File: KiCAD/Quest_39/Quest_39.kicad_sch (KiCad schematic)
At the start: 58 parts, among them J1 1x2 Scr. Term., J10 1x2 Scr. Term., J11 1x2 Scr. Term., J12 Conn_01x05_Male, J2 1x2 Scr. Term., J3 1x2 Scr. Term., J4 1x2 Scr. Term., J5 1x2 Scr. Term., J6 1x2 Scr. Term., J7 1x2 Scr. Term.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

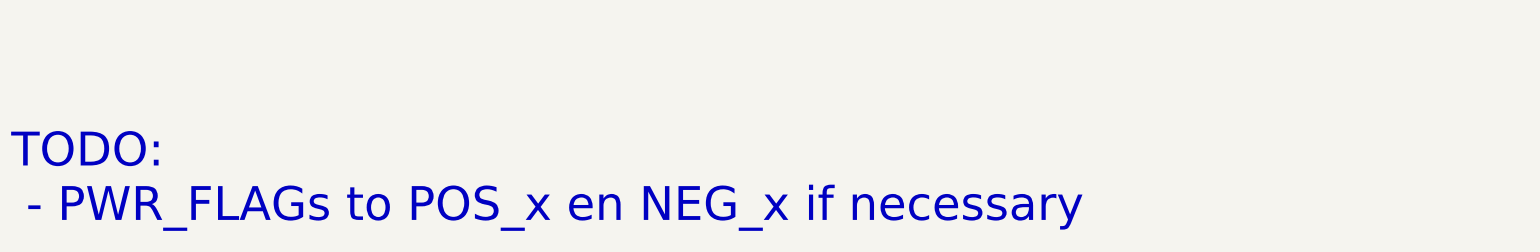
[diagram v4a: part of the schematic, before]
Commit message: Switched to 4-layer stack-up w/ dedicated +5V and GND planes to improve EMI and make routing for PWR-traces easier
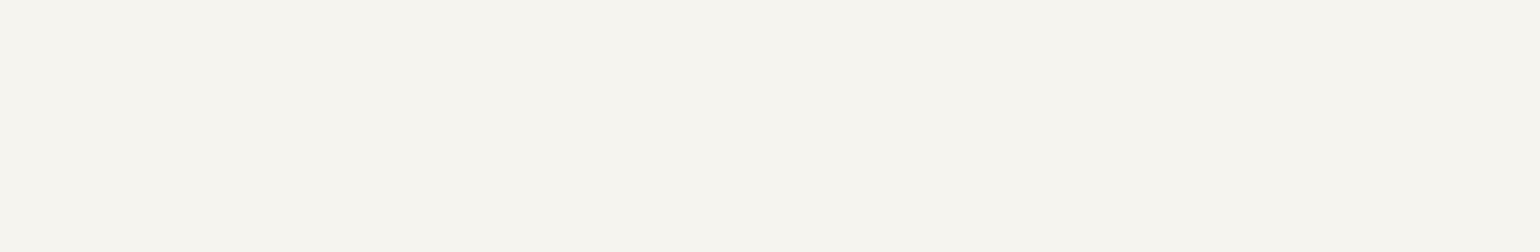
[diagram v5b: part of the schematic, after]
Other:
- note removed: "TODO: - PWR_FLAGs to POS_x en NEG_x if necessary"
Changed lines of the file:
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@@
     (effects (font (size 2.54 2.54) (thickness 0.254) bold) (justify left bottom))
-  )
-  (text "TODO:\n - PWR_FLAGs to POS_x en NEG_x if necessary" (at 13.97 281.94 0)
-    (effects (font (size 6 6)) (justify left bottom))
   )
   (text "SWD\n" (at 132.08 82.55 0)

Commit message: Redid layout for the LTM4611EV Buck-converters (Issues with net-assignment to IC pads)
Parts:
- renumbered J11 to J10, J6 to J11, J7 to J6, J8 to J7, J9 to J8, J10 to J9
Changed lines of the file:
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@@
   (symbol (lib_id "Connector:Screw_Terminal_01x02") (at 254 105.41 0) (unit 1)
     (in_bom yes) (on_board yes)
-    (property "Reference" "J11" (id 0) (at 256.54 105.4099 0)
+    (property "Reference" "J10" (id 0) (at 256.54 105.4099 0)
       (effects (font (size 1.27 1.27)) (justify left))
     )
@@
   (symbol (lib_id "Connector:Screw_Terminal_01x02") (at 254 87.63 0) (unit 1)
     (in_bom yes) (on_board yes)
-    (property "Reference" "J9" (id 0) (at 256.54 87.6299 0)
+    (property "Reference" "J8" (id 0) (at 256.54 87.6299 0)
       (effects (font (size 1.27 1.27)) (justify left))
     )
@@
   (symbol (lib_id "Connector:Screw_Terminal_01x02") (at 364.49 63.5 0) (unit 1)
     (in_bom yes) (on_board yes)
-    (property "Reference" "J6" (id 0) (at 367.03 63.4999 0)
+    (property "Reference" "J11" (id 0) (at 367.03 63.4999 0)
       (effects (font (size 1.27 1.27)) (justify left))
     )
@@
   (symbol (lib_id "Connector:Screw_Terminal_01x02") (at 254 96.52 0) (unit 1)
     (in_bom yes) (on_board yes)
-    (property "Reference" "J10" (id 0) (at 256.54 96.5199 0)
+    (property "Reference" "J9" (id 0) (at 256.54 96.5199 0)
       (effects (font (size 1.27 1.27)) (justify left))
     )
@@
   (symbol (lib_id "Connector:Screw_Terminal_01x02") (at 254 78.74 0) (unit 1)
     (in_bom yes) (on_board yes)
-    (property "Reference" "J8" (id 0) (at 256.54 78.7399 0)
+    (property "Reference" "J7" (id 0) (at 256.54 78.7399 0)
       (effects (font (size 1.27 1.27)) (justify left))
     )
@@
   (symbol (lib_id "Connector:Screw_Terminal_01x02") (at 254 69.85 0) (unit 1)
     (in_bom yes) (on_board yes)
-    (property "Reference" "J7" (id 0) (at 256.54 69.8499 0)
+    (property "Reference" "J6" (id 0) (at 256.54 69.8499 0)
       (effects (font (size 1.27 1.27)) (justify left))
     )
@@
       (reference "J5") (unit 1) (value "1x2 Scr. Term.") (footprint "TB005:TB005-762-02BE")
     )
+    (path "/dff79451-050b-4301-9612-8255e4d0a4c2"
+      (reference "J6") (unit 1) (value "1x2 Scr. Term.") (footprint "TB005:TB005-762-02BE")
+    )
+    (path "/ddfdc362-7411-4278-9142-272fedb7a2a3"
+      (reference "J7") (unit 1) (value "1x2 Scr. Term.") (footprint "TB005:TB005-762-02BE")
+    )
+    (path "/77c9d558-da26-44ef-8991-9b4c76ecd1df"
+      (reference "J8") (unit 1) (value "1x2 Scr. Term.") (footprint "TB005:TB005-762-02BE")
+    )
+    (path "/c6b1c2dc-99c6-4581-9e93-ef553b9a60e7"
+      (reference "J9") (unit 1) (value "1x2 Scr. Term.") (footprint "TB005:TB005-762-02BE")
+    )
+    (path "/6bee6f7d-59ef-4d44-bae2-f37fa2ce899b"
+      (reference "J10") (unit 1) (value "1x2 Scr. Term.") (footprint "TB005:TB005-762-02BE")
+    )
     (path "/b7ec1e0a-09b8-4a1b-a8d2-7b406e266333"
-      (reference "J6") (unit 1) (value "1x2 Scr. Term.") (footprint "TB005:TB005-762-02BE")
-    )
-    (path "/dff79451-050b-4301-9612-8255e4d0a4c2"
-      (reference "J7") (unit 1) (value "1x2 Scr. Term.") (footprint "TB005:TB005-762-02BE")
-    )
-    (path "/ddfdc362-7411-4278-9142-272fedb7a2a3"
-      (reference "J8") (unit 1) (value "1x2 Scr. Term.") (footprint "TB005:TB005-762-02BE")
-    )
-    (path "/77c9d558-da26-44ef-8991-9b4c76ecd1df"
-      (reference "J9") (unit 1) (value "1x2 Scr. Term.") (footprint "TB005:TB005-762-02BE")
-    )
-    (path "/c6b1c2dc-99c6-4581-9e93-ef553b9a60e7"
-      (reference "J10") (unit 1) (value "1x2 Scr. Term.") (footprint "TB005:TB005-762-02BE")
-    )
-    (path "/6bee6f7d-59ef-4d44-bae2-f37fa2ce899b"
       (reference "J11") (unit 1) (value "1x2 Scr. Term.") (footprint "TB005:TB005-762-02BE")
     )
@@
     )
     (path "/b44f6773-e3e8-4e75-9d5c-4dbba7b405cd/74cd0bb3-e3f7-475e-85df-bd98cbcb2213"
-      (reference "U40") (unit 1) (value "AD626ANZ") (footprint "Package_DIP:DIP-8_W8.89mm_SMDSocket_LongPads")
+      (reference "U40") (unit 1) (value "AD626ANZ") (footprint "Package_DIP:DIP-8_W7.62mm_Socket_LongPads")
     )
     (path "/b44f6773-e3e8-4e75-9d5c-4dbba7b405cd/f97e1c91-ef6c-409c-bf4b-77cb96e879ba"

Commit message: Finished routing I2C, SPI and all 10 CS
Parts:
- added TP76, TP77: TestPoint, TestPoint:TestPoint_Pad_D2.0mm, symbol Connector:TestPoint
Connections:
- net SCK: now also TP77.1
- net SCL: now also TP76.1
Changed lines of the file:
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@@
     (stroke (width 0) (type default) (color 0 0 0 0))
   )
-  (wire (pts (xy 171.45 90.17) (xy 184.15 90.17))
+  (wire (pts (xy 171.45 90.17) (xy 186.69 90.17))
     (stroke (width 0) (type default) (color 0 0 0 0))
   )
@@
     (pin "1")
   )
+  (symbol (lib_id "Connector:TestPoint") (at 186.69 90.17 270) (unit 1)
+    (in_bom yes) (on_board yes) (fields_autoplaced)
+    (property "Reference" "TP77" (id 0) (at 191.77 88.8999 90)
+      (effects (font (size 1.27 1.27)) (justify left))
+    )
+    (property "Value" "TestPoint" (id 1) (at 191.77 91.4399 90)
+      (effects (font (size 1.27 1.27)) (justify left))
+    )
+    (property "Footprint" "TestPoint:TestPoint_Pad_D2.0mm" (id 2) (at 186.69 95.25 0)
+      (effects (font (size 1.27 1.27)) hide)
+    )
+    (property "Datasheet" "~" (id 3) (at 186.69 95.25 0)
+      (effects (font (size 1.27 1.27)) hide)
+    )
+    (pin "1")
+  )
   (symbol (lib_id "power:+3.3V") (at 201.93 26.67 0) (unit 1)
     (in_bom yes) (on_board yes)
@@
     (pin "2")
   )
+  (symbol (lib_id "Connector:TestPoint") (at 106.68 92.71 90) (unit 1)
+    (in_bom yes) (on_board yes)
+    (property "Reference" "TP76" (id 0) (at 96.52 90.17 90))
+    (property "Value" "TestPoint" (id 1) (at 96.52 92.71 90))
+    (property "Footprint" "TestPoint:TestPoint_Pad_D2.0mm" (id 2) (at 106.68 87.63 0)
+      (effects (font (size 1.27 1.27)) hide)
+    )
+    (property "Datasheet" "~" (id 3) (at 106.68 87.63 0)
+      (effects (font (size 1.27 1.27)) hide)
+    )
+    (pin "1")
+  )
   (symbol (lib_id "Device:C") (at 355.6 36.83 0) (unit 1)
     (in_bom yes) (on_board yes) (fields_autoplaced)
@@
       (reference "TP75") (unit 1) (value "TestPoint") (footprint "TestPoint:TestPoint_Pad_D2.0mm")
     )
+    (path "/40a87cde-b297-4d31-a926-c458c0a5be97"
+      (reference "TP76") (unit 1) (value "TestPoint") (footprint "TestPoint:TestPoint_Pad_D2.0mm")
+    )
+    (path "/061ab18d-bcf6-4d4a-a6ad-8b400acdd03b"
+      (reference "TP77") (unit 1) (value "TestPoint") (footprint "TestPoint:TestPoint_Pad_D2.0mm")
+    )
     (path "/3744030b-c48a-48bd-a5cf-c353ea25d475"

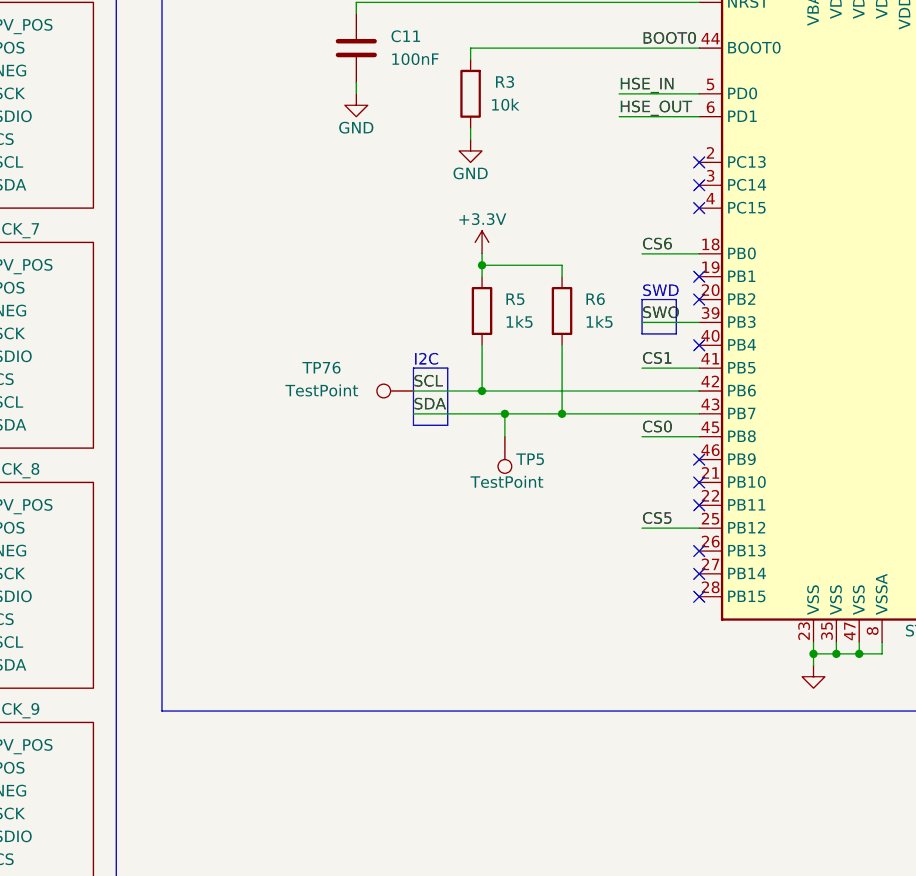
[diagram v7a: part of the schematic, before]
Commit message: Added MOSFET bi-directional level-shifters to fix I2C between INA226's and STM32F103. Fixed mismatched via sizes.
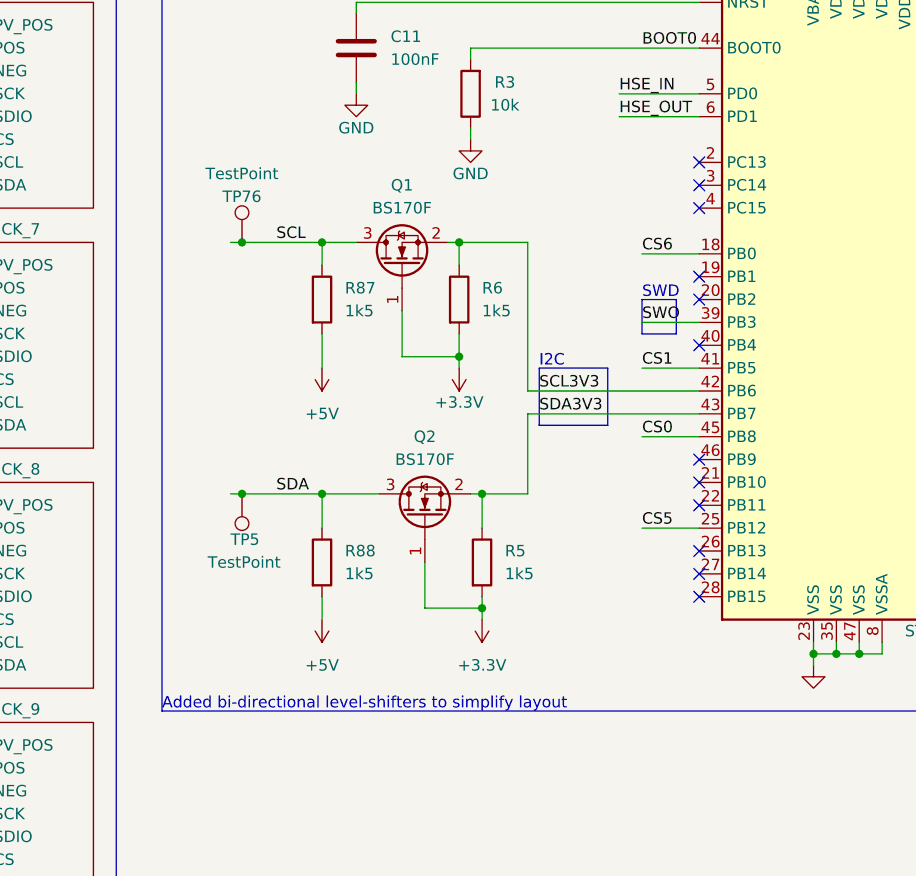
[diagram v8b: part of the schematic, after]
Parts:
- added Q1, Q2: BS170F, Package_TO_SOT_SMD:SOT-23, symbol Transistor_FET:BS170F
- added R87, R88: 1k5, Resistor_SMD:R_0805_2012Metric, symbol Device:R
- R5, R6: footprint Resistor_SMD:R_1206_3216Metric -> Resistor_SMD:R_0805_2012Metric
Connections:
- net +3.3V: now also R5.2, R6.2, Q1.1 (G), Q2.1 (G); no longer R5.1, R6.1
- net +5V: now also R87.2, R88.2
- net SCL: now also Q1.3 (D), R87.1; no longer R5.2, U3.42 (PB6)
- net SDA: now also Q2.3 (D), R88.1; no longer R6.2, U3.43 (PB7)
- new net SCL3V3: Q1.2 (S), R6.1, U3.42 (PB6)
- new net SDA3V3: Q2.2 (S), R5.1, U3.43 (PB7)
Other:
- note added: "Added bi-directional level-shifters to simplify layout"
- moved on the sheet: R5, R6, TP5, TP76
